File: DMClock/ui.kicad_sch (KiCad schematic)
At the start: 36 parts, among them SW1 SW_Push, SW2 SW_Push, SW3 SW_Push, SW4 SW_SP3T (power toggle)

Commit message: adding mplabxide init files
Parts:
- SW4: value SW_SP3T (power toggle) -> SW_SP3T (mode select)
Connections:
- net GND: no longer SW4.2
- net 9V: no longer names the net of SW4.3
- net Barrel Jack: no longer names the net of SW4.1
- net Battery: no longer names the net of SW4.4
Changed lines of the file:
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@@
     (effects (font (size 1.27 1.27)) (justify left bottom))
-  )
-  (hierarchical_label "Barrel Jack" (shape input) (at 244.221 69.215 270) (fields_autoplaced)
-    (effects (font (size 1.27 1.27)) (justify right))
   )
   (hierarchical_label "HV" (shape input) (at 138.811 106.426 0) (fields_autoplaced)
@@
     (effects (font (size 1.27 1.27)) (justify left))
   )
-  (hierarchical_label "Battery" (shape input) (at 239.141 69.215 270) (fields_autoplaced)
-    (effects (font (size 1.27 1.27)) (justify right))
-  )
   (hierarchical_label "HV" (shape input) (at 138.049 168.91 0) (fields_autoplaced)
     (effects (font (size 1.27 1.27)) (justify left))
@@
     (effects (font (size 1.27 1.27)) (justify left))
   )
-  (hierarchical_label "9V" (shape input) (at 241.681 59.055 90) (fields_autoplaced)
-    (effects (font (size 1.27 1.27)) (justify left))
-  )
   (hierarchical_label "HV" (shape input) (at 94.869 169.418 0) (fields_autoplaced)
     (effects (font (size 1.27 1.27)) (justify left))
@@
         (path "/b42b345f-a3f2-4eff-9109-2f4619119d33/6e102def-f8db-44ea-948b-b7115f90d225"
           (reference "#PWR019") (unit 1)
-        )
-      )
-    )
-  )
-  (symbol (lib_id "power:GND") (at 241.681 69.215 0) (unit 1)
-    (in_bom yes) (on_board yes) (dnp no) (fields_autoplaced)
-    (property "Reference" "#PWR026" (at 241.681 75.565 0)
-      (effects (font (size 1.27 1.27)) hide)
-    )
-    (property "Value" "GND" (at 241.681 73.533 0)
-      (effects (font (size 1.27 1.27)))
-    )
-    (property "Footprint" "" (at 241.681 69.215 0)
-      (effects (font (size 1.27 1.27)) hide)
-    )
-    (property "Datasheet" "" (at 241.681 69.215 0)
-      (effects (font (size 1.27 1.27)) hide)
-    )
-    (pin "1")
-    (instances
-      (project "DMClock"
-        (path "/b42b345f-a3f2-4eff-9109-2f4619119d33/6e102def-f8db-44ea-948b-b7115f90d225"
-          (reference "#PWR026") (unit 1)
         )
       )
@@
       (effects (font (size 1.27 1.27)) (justify left))
     )
-    (property "Value" "SW_SP3T (power toggle)" (at 246.38 65.405 90)
+    (property "Value" "SW_SP3T (mode select)" (at 246.38 65.405 90)
       (effects (font (size 1.27 1.27)) (justify left))
     )

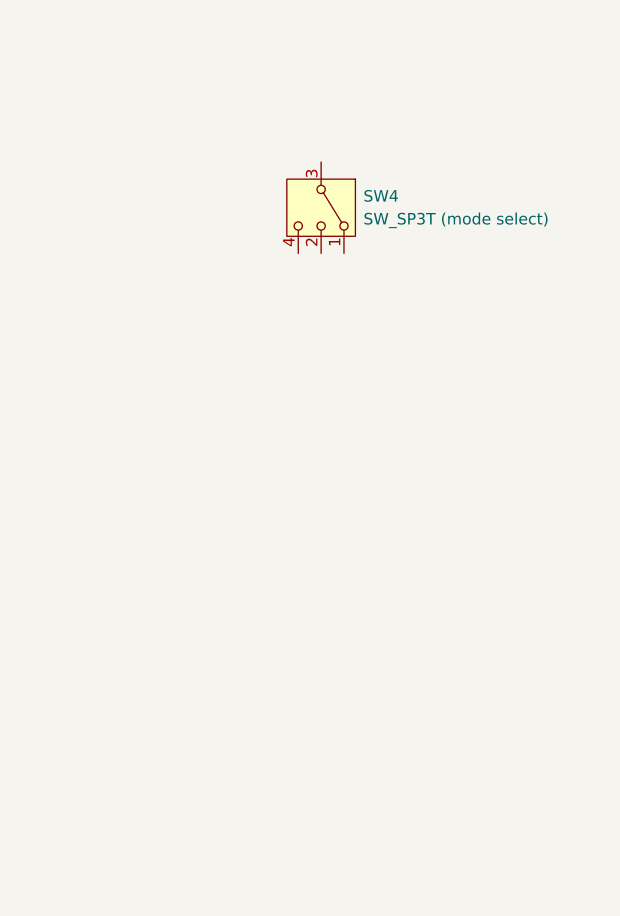
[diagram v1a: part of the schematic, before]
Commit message: more modules added, still need to add a lot of footprints and see if there exist any sd card libraries for use with i2s
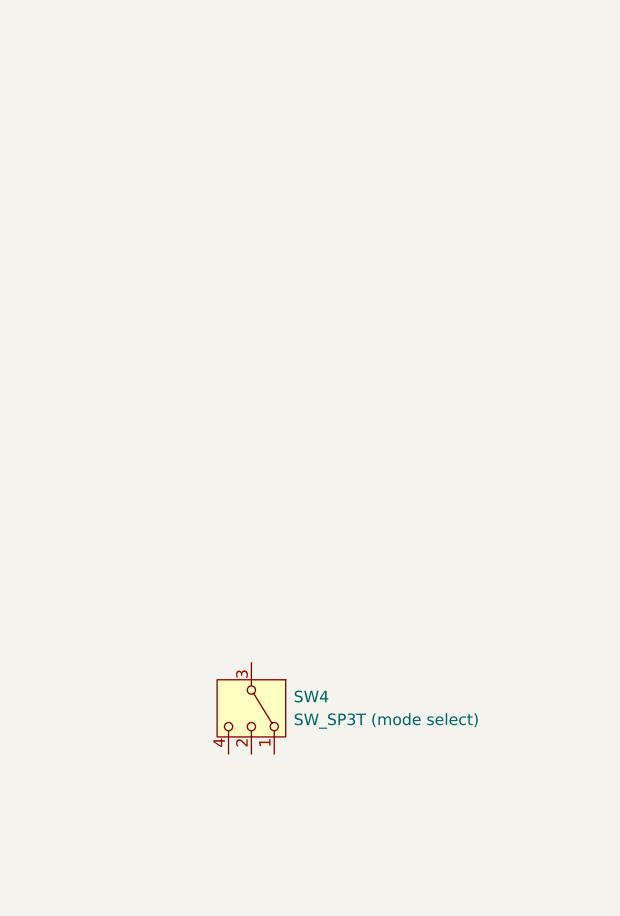
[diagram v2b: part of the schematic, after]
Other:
- moved on the sheet: SW4
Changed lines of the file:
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@@
     )
   )
-  (symbol (lib_id "Switch:SW_SP3T") (at 241.681 64.135 270) (unit 1)
+  (symbol (lib_id "Switch:SW_SP3T") (at 233.934 119.761 270) (unit 1)
     (in_bom yes) (on_board yes) (dnp no) (fields_autoplaced)
-    (property "Reference" "SW4" (at 246.38 62.865 90)
+    (property "Reference" "SW4" (at 238.633 118.491 90)
       (effects (font (size 1.27 1.27)) (justify left))
     )
-    (property "Value" "SW_SP3T (mode select)" (at 246.38 65.405 90)
+    (property "Value" "SW_SP3T (mode select)" (at 238.633 121.031 90)
       (effects (font (size 1.27 1.27)) (justify left))
     )
-    (property "Footprint" "" (at 246.126 48.26 0)
+    (property "Footprint" "" (at 238.379 103.886 0)
       (effects (font (size 1.27 1.27)) hide)
     )
-    (property "Datasheet" "~" (at 234.061 64.135 0)
+    (property "Datasheet" "~" (at 226.314 119.761 0)
       (effects (font (size 1.27 1.27)) hide)
     )

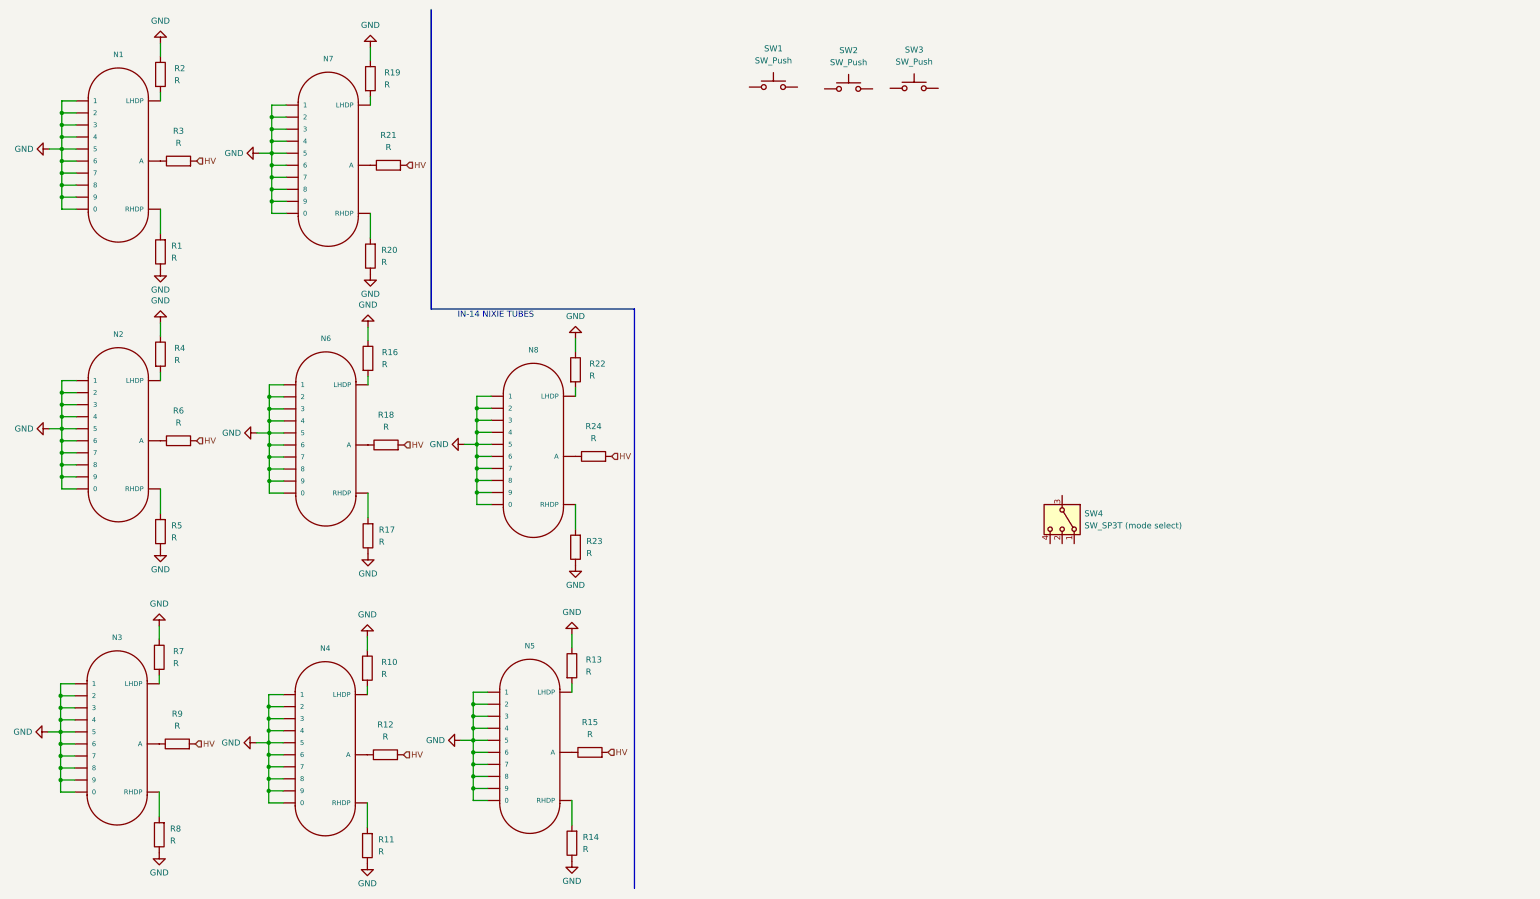
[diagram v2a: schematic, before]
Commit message: added more to schematic, hv622
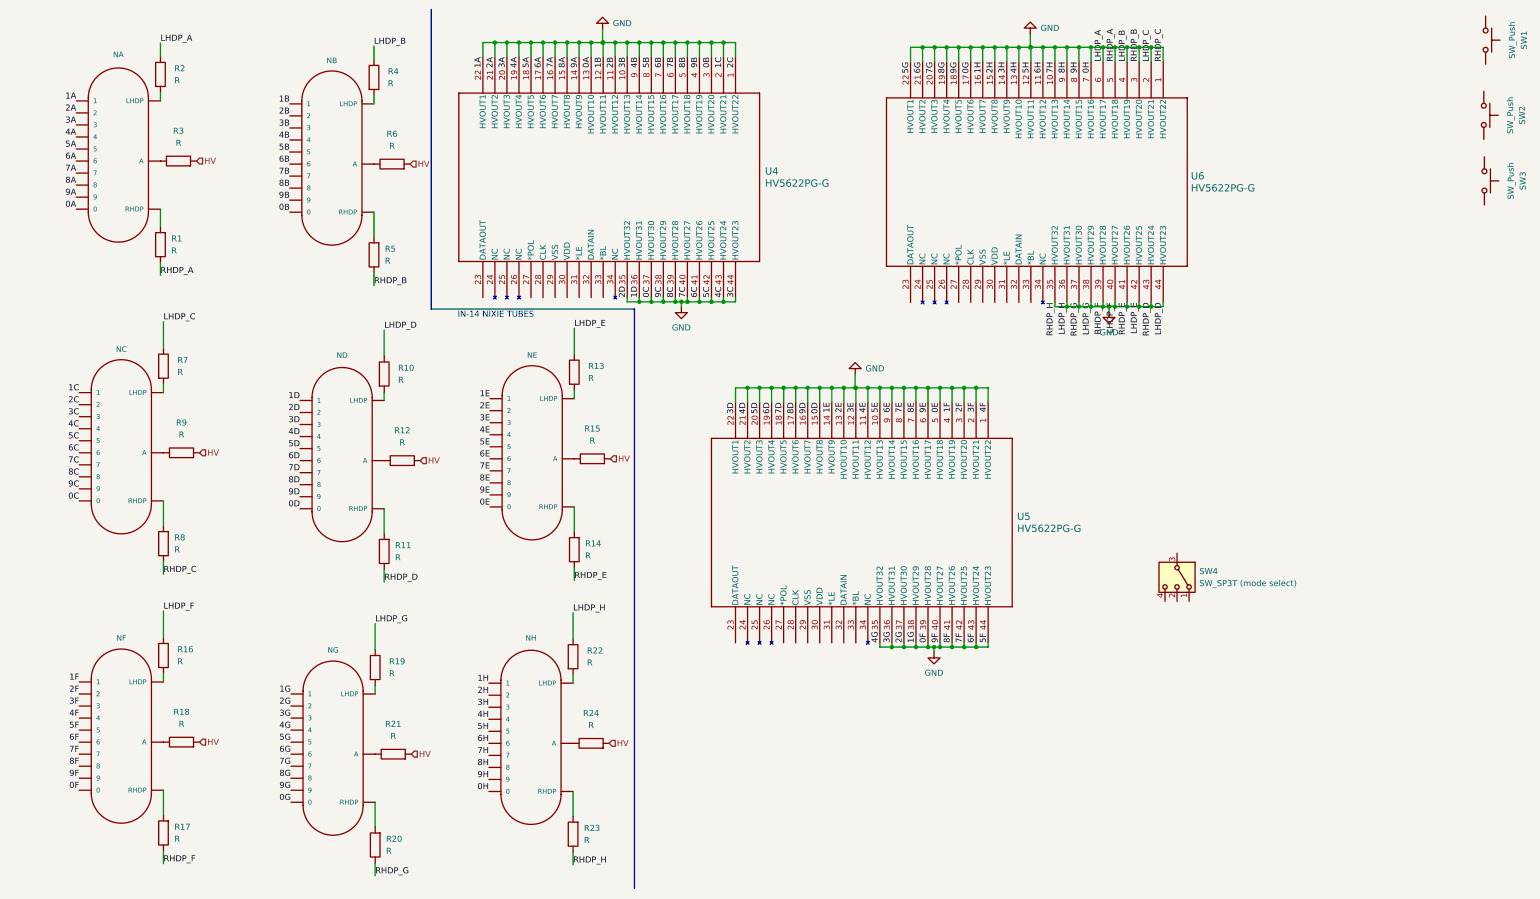
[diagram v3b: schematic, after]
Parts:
- added U4, U5, U6: HV5622PG-G, Footprints:QFP44_10x10MC_MCH, symbol 2024-06-14_08-02-32:HV5622PG-G
- renumbered N1 to NA, N2 to NB, N3 to NC, N4 to ND, N5 to NE, N6 to NF, N7 to NG, N8 to NH
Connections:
- net GND: now also U4.1 (HVOUT22), U4.10 (HVOUT13), U4.11 (HVOUT12), U4.12 (HVOUT11), U4.13 (HVOUT10), U4.14 (HVOUT9), U4.15 (HVOUT8), U4.16 (HVOUT7), U4.17 (HVOUT6), U4.18 (HVOUT5), U4.19 (HVOUT4), U4.2 (HVOUT21), U4.20 (HVOUT3), U4.21 (HVOUT2), U4.22 (HVOUT1), U4.3 (HVOUT20), U4.35 (HVOUT32), U4.36 (HVOUT31), U4.37 (HVOUT30), U4.38 (HVOUT29), U4.39 (HVOUT28), U4.4 (HVOUT19), U4.40 (HVOUT27), U4.41 (HVOUT26), U4.42 (HVOUT25), U4.43 (HVOUT24), U4.44 (HVOUT23), U4.5 (HVOUT18), U4.6 (HVOUT17), U4.7 (HVOUT16), U4.8 (HVOUT15), U4.9 (HVOUT14), U5.1 (HVOUT22), U5.10 (HVOUT13), U5.11 (HVOUT12), U5.12 (HVOUT11), U5.13 (HVOUT10), U5.14 (HVOUT9), U5.15 (HVOUT8), U5.16 (HVOUT7), U5.17 (HVOUT6), U5.18 (HVOUT5), U5.19 (HVOUT4), U5.2 (HVOUT21), U5.20 (HVOUT3), U5.21 (HVOUT2), U5.22 (HVOUT1), U5.3 (HVOUT20), U5.35 (HVOUT32), U5.36 (HVOUT31), U5.37 (HVOUT30), U5.38 (HVOUT29), U5.39 (HVOUT28), U5.4 (HVOUT19), U5.40 (HVOUT27), U5.41 (HVOUT26), U5.42 (HVOUT25), U5.43 (HVOUT24), U5.44 (HVOUT23), U5.5 (HVOUT18), U5.6 (HVOUT17), U5.7 (HVOUT16), U5.8 (HVOUT15), U5.9 (HVOUT14), U6.1 (HVOUT22), U6.10 (HVOUT13), U6.11 (HVOUT12), U6.12 (HVOUT11), U6.13 (HVOUT10), U6.14 (HVOUT9), U6.15 (HVOUT8), U6.16 (HVOUT7), U6.17 (HVOUT6), U6.18 (HVOUT5), U6.19 (HVOUT4), U6.2 (HVOUT21), U6.20 (HVOUT3), U6.21 (HVOUT2), U6.22 (HVOUT1), U6.3 (HVOUT20), U6.35 (HVOUT32), U6.36 (HVOUT31), U6.37 (HVOUT30), U6.38 (HVOUT29), U6.39 (HVOUT28), U6.4 (HVOUT19), U6.40 (HVOUT27), U6.41 (HVOUT26), U6.42 (HVOUT25), U6.43 (HVOUT24), U6.44 (HVOUT23), U6.5 (HVOUT18), U6.6 (HVOUT17), U6.7 (HVOUT16), U6.8 (HVOUT15), U6.9 (HVOUT14)
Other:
- moved on the sheet: NB, NC, ND, NE, NF, NG, NH, R1, R10, R11, R12, R13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

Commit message: need to work on hvps logic converter
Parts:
- renumbered NA to NA1, NB to NB1, NC to NC1, ND to ND1, NE to NE1, NF to NF1, NG to NG1, NH to NH1, R2 to R10, R1 to R11, R7 to R12, R8 to R13, R16 to R14, R17 to R15, R3 to R16, R9 to R17, R4 to R19, R5 to R20, R19 to R21, R20 to R22, R10 to R23, R11 to R24, R6 to R25, R21 to R26, R12 to R27, R22 to R28, R23 to R29, R13 to R30, R14 to R31, R24 to R32, R15 to R33, SW4 to SW3, SW2 to SW4, SW3 to SW5, SW1 to SW6, U4 to U3, U6 to U4
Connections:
- net GND: now also U3.29 (VSS), U4.29 (VSS), U5.29 (VSS)
- net CLK: now reaches U4.28 (CLK)
- net CLK: now also U3.28 (CLK), U5.28 (CLK)
- net 12V: now reaches U4.30 (VDD)
- net 12V: now also U3.30 (VDD), U5.30 (VDD)
- net NOTLE: now reaches U4.31 (*LE)
- net NOTLE: now also U3.31 (*LE), U5.31 (*LE)
- net DATA2OUT: now reaches U4.32 (DATAIN)
- net DATA2OUT: now also U5.23 (DATAOUT)
- net NOTBL: now reaches U4.33 (*BL)
- net NOTBL: now also U3.33 (*BL), U5.33 (*BL)
- net DATA1OUT: now reaches U5.32 (DATAIN)
- net DATA1OUT: now also U3.23 (DATAOUT)
- net HV5622DataIn: now reaches U3.32 (DATAIN)
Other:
- moved on the sheet: U4, U5

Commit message: just need to finish pcb
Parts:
- removed SW3: SW_SP3T (mode select), symbol Switch:SW_SP3T
- removed SW4, SW5, SW6: SW_Push, symbol Switch:SW_Push
- added C12, C13, C14: 0.1uF, Capacitor_SMD:C_0805_2012Metric, symbol Device:C
- added TP1, TP10, TP100, TP101, TP102, TP103, TP104, TP11, TP12, TP13, TP14, TP15, TP16, TP17, TP18, TP19, TP2, TP20, TP21, TP22, TP23, TP24, TP25, TP26, TP27, TP28, TP29, TP3, TP30, TP31, TP32, TP33, TP34, TP35, TP36, TP37, TP38, TP39, TP4, TP40, TP41, TP42, TP43, TP44, TP45, TP46, TP47, TP48, TP49, TP5, TP50, TP51, TP52, TP53, TP54, TP55, TP56, TP57, TP58, TP59, TP6, TP60, TP61, TP62, TP63, TP64, TP65, TP66, TP67, TP68, TP69, TP7, TP70, TP71, TP72, TP73, TP74, TP75, TP76, TP77, TP78, TP79, TP8, TP80, TP81, TP82, TP83, TP84, TP85, TP86, TP87, TP88, TP89, TP9, TP90, TP91, TP92, TP93, TP94, TP95, TP96, TP97, TP98, TP99: TestPoint, TestPoint:TestPoint_Pad_D1.5mm, symbol Connector:TestPoint
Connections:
- net 12V: now also U3.27 (*POL), U4.27 (*POL), U5.27 (*POL), C12.1, C13.1, C14.1
- net GND: now also C12.2, C13.2, C14.2, TP1.1, TP10.1, TP11.1, TP12.1, TP13.1, TP14.1, TP15.1, TP16.1, TP17.1, TP18.1, TP19.1, TP2.1, TP20.1, TP21.1, TP22.1, TP23.1, TP24.1, TP25.1, TP26.1, TP27.1, TP28.1, TP29.1, TP3.1, TP30.1, TP31.1, TP32.1, TP33.1, TP34.1, TP35.1, TP36.1, TP37.1, TP38.1, TP39.1, TP4.1, TP40.1, TP41.1, TP42.1, TP43.1, TP44.1, TP45.1, TP46.1, TP47.1, TP48.1, TP49.1, TP5.1, TP50.1, TP51.1, TP52.1, TP53.1, TP54.1, TP55.1, TP56.1, TP57.1, TP58.1, TP59.1, TP6.1, TP60.1, TP61.1, TP62.1, TP63.1, TP64.1, TP65.1, TP66.1, TP67.1, TP68.1, TP69.1, TP7.1, TP70.1, TP71.1, TP72.1, TP73.1, TP74.1, TP75.1, TP76.1, TP77.1, TP78.1, TP79.1, TP8.1, TP80.1, TP81.1, TP82.1, TP83.1, TP84.1, TP85.1, TP86.1, TP87.1, TP88.1, TP89.1, TP9.1, TP90.1, TP91.1, TP92.1, TP93.1, TP94.1, TP95.1, TP96.1
- net at NA1.A, R16.1: now also TP100.1
- net at NB1.A, R25.1: now also TP99.1
- net at NH1.A, R32.1: now also TP104.1
- net at NC1.A, R17.1: now also TP101.1
- net at NE1.A, R33.1: now also TP98.1
- net at ND1.A, R27.1: now also TP97.1
- net at NF1.A, R18.1: now also TP102.1
- net at NG1.A, R26.1: now also TP103.1
